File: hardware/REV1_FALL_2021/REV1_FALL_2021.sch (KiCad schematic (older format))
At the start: 22 parts, among them U1 Teensy3.6_All_Pins, U2 PA16165_Breakout, U3 MPL3115A2_Breakout, U4 BNO055_Breakout, U5 RFM69HCW_Breakout

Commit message: arrange and annotate schematic
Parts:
- removed BT? (x2): Battery_Cell, symbol Device:Battery_Cell
- removed C? (x2): C_0.1uF, symbol Device:C
- removed C?: C, symbol Device:C
- removed R?: R_250, symbol Device:R
- removed R?: R_15k, symbol Device:R
- removed R?: R_5k, symbol Device:R
- removed R?: R_10k, symbol Device:R
- removed U?: TPS2113ADRBR, IC_DRV8601DRBT, symbol TPS2113ADRBR:TPS2113ADRBR
- gave numbers to parts that had none: 7
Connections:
- net E-Match_Trigger_1 is gone; now on net E-MATCH_TRIGGER: R103.2
- net STAT is gone; now on net TPS_1_STAT: U1.32 (35_A16_PWM)
- net VIN is gone; now on net V_TEENSY: U1.53 (VIN)
- net BALANCE_CONTROL: now also U1.34 (37_A18_PWM_SCL1)
- net TPS_2_STAT: now also U1.33 (36_A17_PWM)
- net E-MATCH_TRIGGER: now reaches U1.36 (39_A20)
- no-connect marks 89 -> 88
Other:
- moved on the sheet: BT101, BT102, J101, Q101, R101, R102, R103, U1

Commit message: assign footprints to all but battery holders
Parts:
- R101, R102, R103: footprint (none) -> Resistor_SMD:R_0805_2012Metric_Pad1.20x1.40mm_HandSolder
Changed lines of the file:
@@
 F 0 "R103" V 19343 4400 50  0000 C CNN
 F 1 "R_10k" V 19434 4400 50  0000 C CNN
-F 2 "" V 19480 4400 50  0001 C CNN
+F 2 "Resistor_SMD:R_0805_2012Metric_Pad1.20x1.40mm_HandSolder" V 19480 4400 50  0001 C CNN
 F 3 "~" H 19550 4400 50  0001 C CNN
 	1    19550 4400
@@
 F 0 "R102" H 14220 6796 50  0000 L CNN
 F 1 "R_5k" H 13900 6750 50  0000 L CNN
-F 2 "" V 14080 6750 50  0001 C CNN
+F 2 "Resistor_SMD:R_0805_2012Metric_Pad1.20x1.40mm_HandSolder" V 14080 6750 50  0001 C CNN
 F 3 "~" H 14150 6750 50  0001 C CNN
 	1    14150 6750
@@
 F 0 "R101" H 14220 6196 50  0000 L CNN
 F 1 "R_15k" H 13850 6150 50  0000 L CNN
-F 2 "" V 14080 6150 50  0001 C CNN
+F 2 "Resistor_SMD:R_0805_2012Metric_Pad1.20x1.40mm_HandSolder" V 14080 6150 50  0001 C CNN
 F 3 "~" H 14150 6150 50  0001 C CNN
 	1    14150 6150

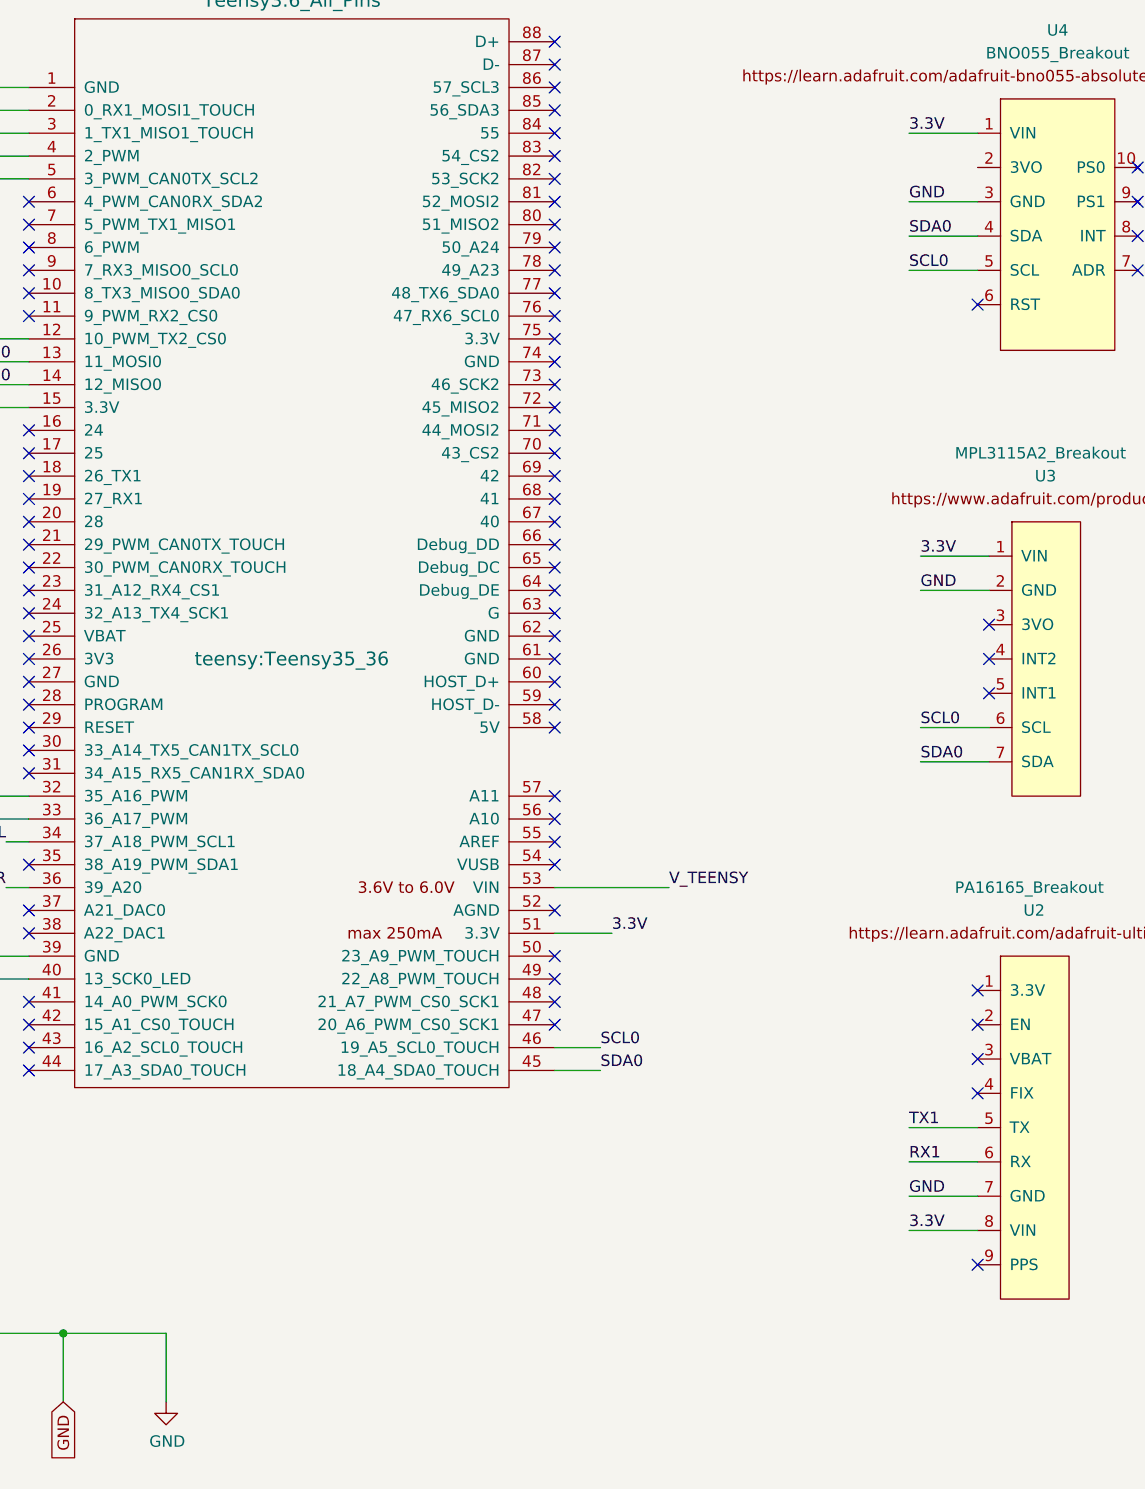
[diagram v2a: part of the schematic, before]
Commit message: import and associate battery footprint
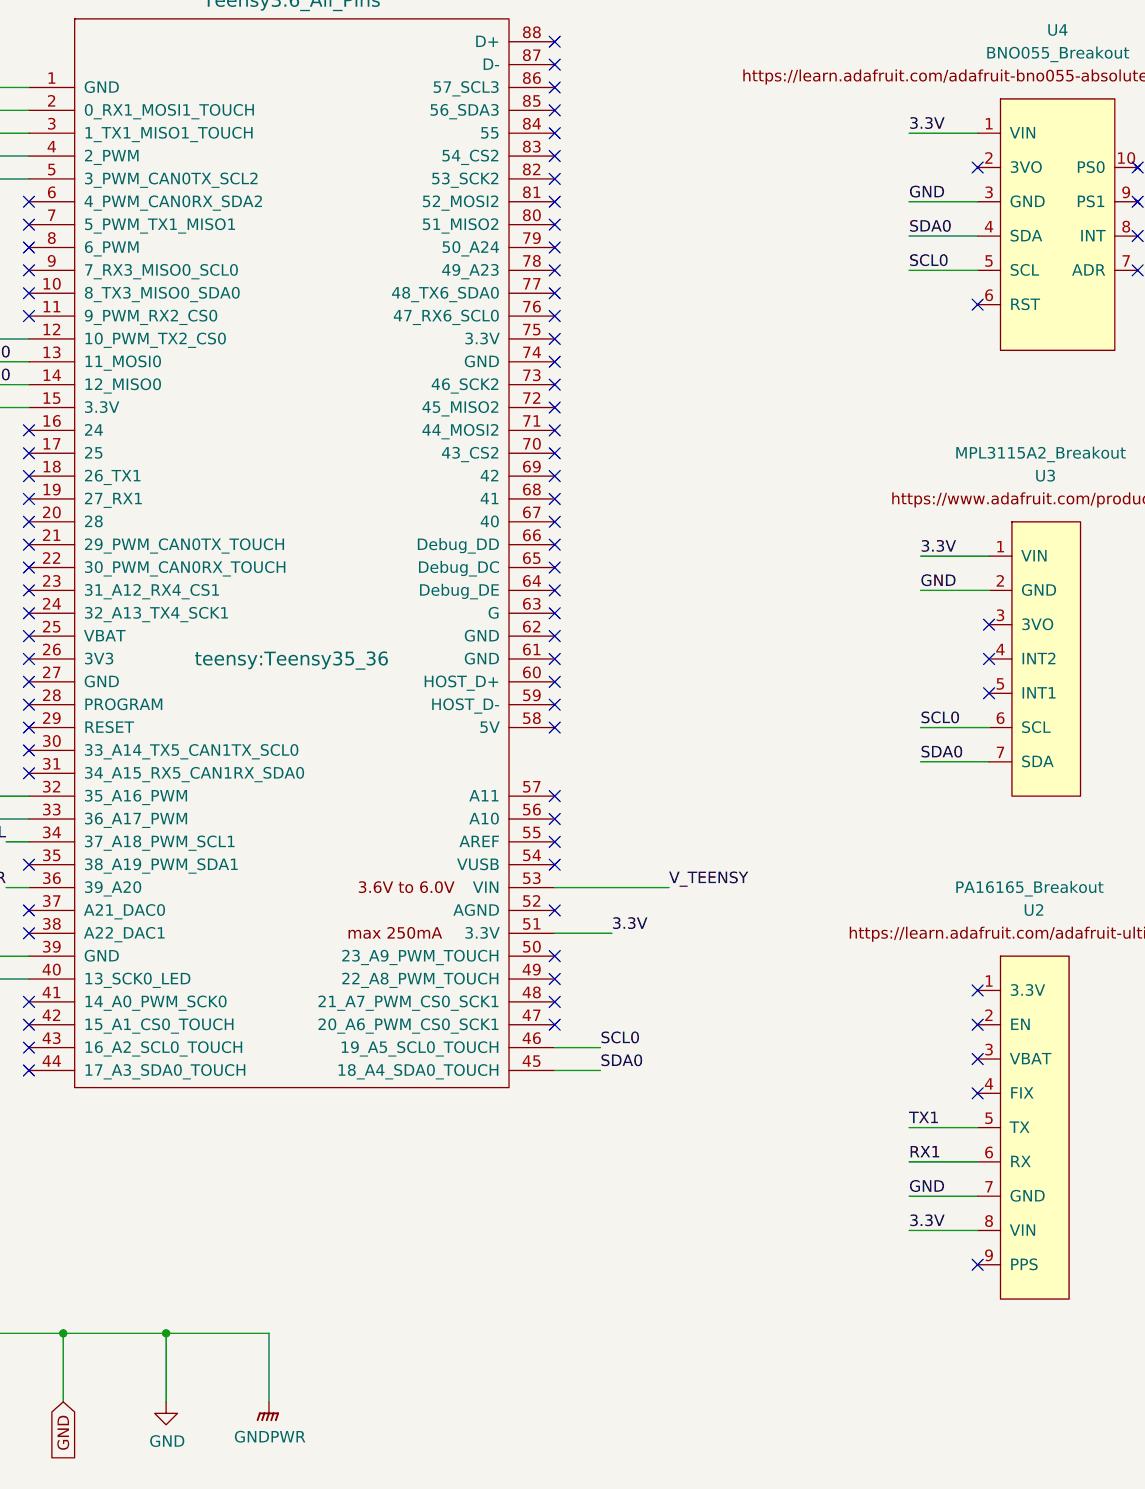
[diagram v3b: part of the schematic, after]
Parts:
- BT101, BT102: footprint (none) -> Olin_Rocketry:MyBatteryHolder_MPD_BH-18650-PC2
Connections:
- no-connect marks 88 -> 89
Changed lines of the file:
@@
 F 0 "BT101" H 12968 4446 50  0000 L CNN
 F 1 "Battery_Cell" H 12968 4355 50  0000 L CNN
-F 2 "" V 12850 4410 50  0001 C CNN
+F 2 "Olin_Rocketry:MyBatteryHolder_MPD_BH-18650-PC2" V 12850 4410 50  0001 C CNN
 F 3 "~" V 12850 4410 50  0001 C CNN
 	1    12850 4350
@@
 F 0 "BT102" H 13018 3596 50  0000 L CNN
 F 1 "Battery_Cell" H 13018 3505 50  0000 L CNN
-F 2 "" V 12900 3560 50  0001 C CNN
+F 2 "Olin_Rocketry:MyBatteryHolder_MPD_BH-18650-PC2" V 12900 3560 50  0001 C CNN
 F 3 "~" V 12900 3560 50  0001 C CNN
 	1    12900 3500
@@
 NoConn ~ 3750 2550
 NoConn ~ 3750 2650
+NoConn ~ 5600 1800
+$Comp
+L power:GNDPWR #PWR0101
+U 1 1 61B2C185
+P 2500 7200
+F 0 "#PWR0101" H 2500 7000 50  0001 C CNN
+F 1 "GNDPWR" H 2504 7046 50  0000 C CNN
+F 2 "" H 2500 7150 50  0001 C CNN
+F 3 "" H 2500 7150 50  0001 C CNN
+	1    2500 7200
+	1    0    0    -1
+$EndComp
+Wire Wire Line
+	2500 7200 2500 6900
+Wire Wire Line
+	2500 6900 2050 6900
+Connection ~ 2050 6900
 $EndSCHEMATC

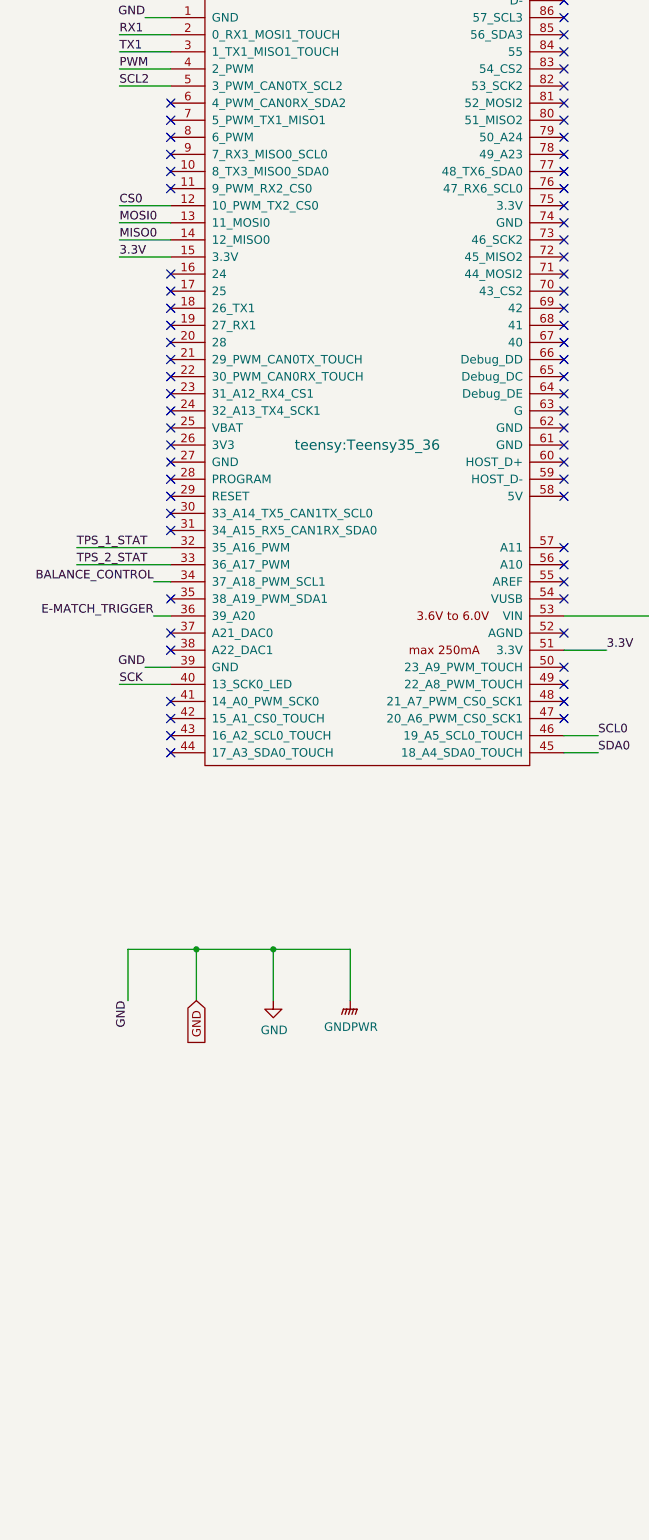
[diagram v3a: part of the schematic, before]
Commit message: add LEDs to schematic
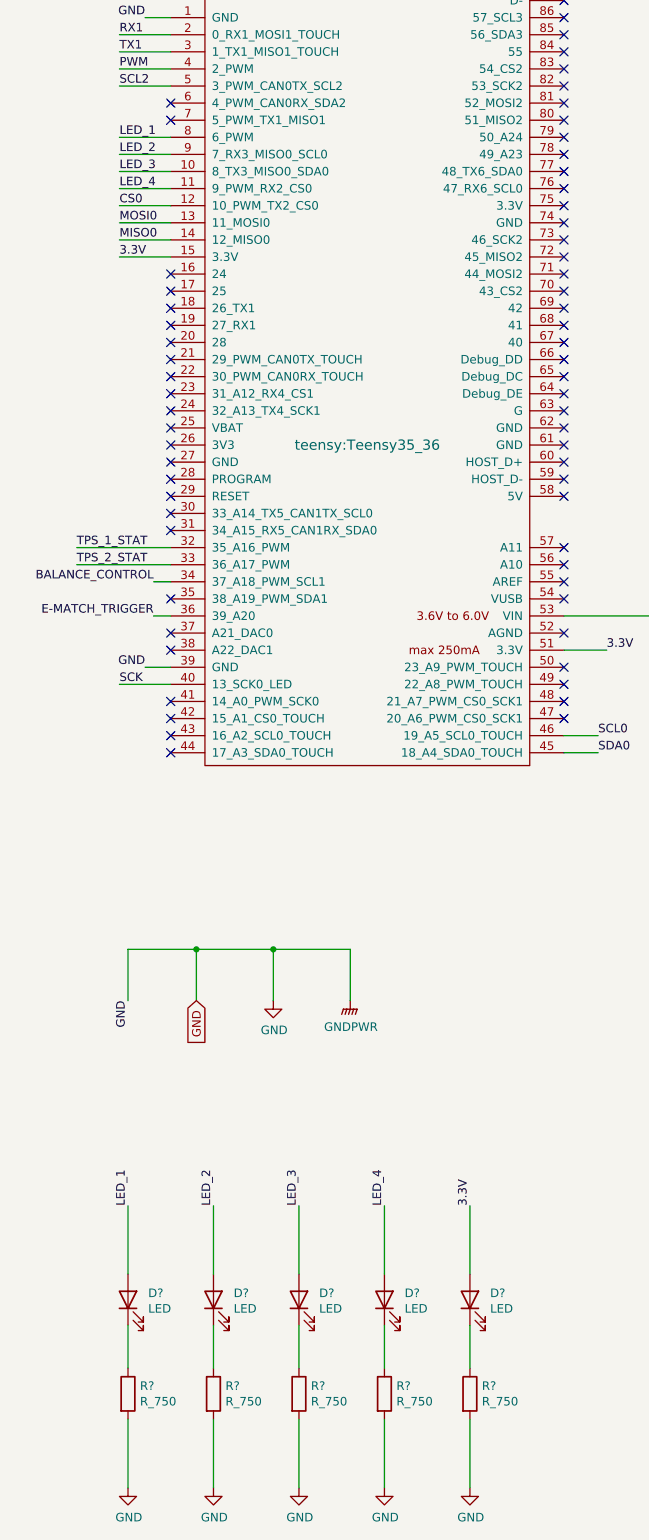
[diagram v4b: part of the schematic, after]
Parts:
- added D? (x5): LED, LED_SMD:LED_0805_2012Metric_Pad1.15x1.40mm_HandSolder, symbol Device:LED
- added R? (x5): R_750, Resistor_SMD:R_0805_2012Metric_Pad1.20x1.40mm_HandSolder, symbol Device:R
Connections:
- net 3.3V: now also D?.2 (A)
- net GND: now also R?.2, R?.2, R?.2, R?.2, R?.2
- net LED_3: now reaches U1.10 (8_TX3_MISO0_SDA0)
- net LED_3: now also D?.2 (A)
- net LED_4: now reaches U1.11 (9_PWM_RX2_CS0)
- net LED_4: now also D?.2 (A)
- net LED_1: now reaches U1.8 (6_PWM)
- net LED_1: now also D?.2 (A)
- net LED_2: now reaches U1.9 (7_RX3_MISO0_SCL0)
- net LED_2: now also D?.2 (A)
- new net: D?.1 (K), R?.1 (x5)
- no-connect marks 89 -> 85
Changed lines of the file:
@@
 NoConn ~ 1450 1950
 NoConn ~ 1450 2050
-NoConn ~ 1450 2150
-NoConn ~ 1450 2250
-NoConn ~ 1450 2350
-NoConn ~ 1450 2450
 NoConn ~ 1450 2950
 NoConn ~ 1450 3050
@@
 	2500 6900 2050 6900
 Connection ~ 2050 6900
+$Comp
+L Device:LED D?
+U 1 1 619C7C94
+P 1200 8950
+F 0 "D?" V 1239 8832 50  0000 R CNN
+F 1 "LED" V 1148 8832 50  0000 R CNN
+F 2 "LED_SMD:LED_0805_2012Metric_Pad1.15x1.40mm_HandSolder" H 1200 8950 50  0001 C CNN
+F 3 "https://datasheet.lcsc.com/lcsc/1806130620_Hubei-KENTO-Elec-C2293_C2293.pdf" H 1200 8950 50  0001 C CNN
+	1    1200 8950
+	0    -1   -1   0
+$EndComp
+$Comp
+L Device:R R?
+U 1 1 619CBBB6
+P 1200 9500
+F 0 "R?" H 1270 9546 50  0000 L CNN
+F 1 "R_750" H 1270 9455 50  0000 L CNN
+F 2 "Resistor_SMD:R_0805_2012Metric_Pad1.20x1.40mm_HandSolder" V 1130 9500 50  0001 C CNN
+F 3 "~" H 1200 9500 50  0001 C CNN
+	1    1200 9500
+	1    0    0    -1
+$EndComp
+Wire Wire Line
+	1200 9100 1200 9350
+Text Label 1200 8400 1    50   ~ 0
+LED_1
+Wire Wire Line
+	1200 8400 1200 8800
+Wire Wire Line
+	1200 9650 1200 10050
+$Comp
+L power:GND #PWR?
+U 1 1 619E5D47
+P 1200 10050
+F 0 "#PWR?" H 1200 9800 50  0001 C CNN
+F 1 "GND" H 1205 9877 50  0000 C CNN
+F 2 "" H 1200 10050 50  0001 C CNN
+F 3 "" H 1200 10050 50  0001 C CNN
+	1    1200 10050
+	1    0    0    -1
+$EndComp
+$Comp
+L Device:LED D?
+U 1 1 619E9614
+P 1700 8950
+F 0 "D?" V 1739 8832 50  0000 R CNN
+F 1 "LED" V 1648 8832 50  0000 R CNN
+F 2 "LED_SMD:LED_0805_2012Metric_Pad1.15x1.40mm_HandSolder" H 1700 8950 50  0001 C CNN
+F 3 "https://datasheet.lcsc.com/lcsc/1806130620_Hubei-KENTO-Elec-C2293_C2293.pdf" H 1700 8950 50  0001 C CNN
+	1    1700 8950
+	0    -1   -1   0
+$EndComp
+$Comp
+L Device:R R?
+U 1 1 619E961A
+P 1700 9500
+F 0 "R?" H 1770 9546 50  0000 L CNN
+F 1 "R_750" H 1770 9455 50  0000 L CNN
+F 2 "Resistor_SMD:R_0805_2012Metric_Pad1.20x1.40mm_HandSolder" V 1630 9500 50  0001 C CNN
+F 3 "~" H 1700 9500 50  0001 C CNN
+	1    1700 9500
+	1    0    0    -1
+$EndComp
+Wire Wire Line
+	1700 9100 1700 9350
+Text Label 1700 8400 1    50   ~ 0
+LED_2
+Wire Wire Line
+	1700 8400 1700 8800
+Wire Wire Line
+	1700 9650 1700 10050
+$Comp
+L power:GND #PWR?
+U 1 1 619E9624
+P 1700 10050
+F 0 "#PWR?" H 1700 9800 50  0001 C CNN
+F 1 "GND" H 1705 9877 50  0000 C CNN
+F 2 "" H 1700 10050 50  0001 C CNN
+F 3 "" H 1700 10050 50  0001 C CNN
+	1    1700 10050
+	1    0    0    -1
+$EndComp
+$Comp
+L Device:LED D?
+U 1 1 619EBAF0
+P 2200 8950
+F 0 "D?" V 2239 8832 50  0000 R CNN
+F 1 "LED" V 2148 8832 50  0000 R CNN
+F 2 "LED_SMD:LED_0805_2012Metric_Pad1.15x1.40mm_HandSolder" H 2200 8950 50  0001 C CNN
+F 3 "https://datasheet.lcsc.com/lcsc/1806130620_Hubei-KENTO-Elec-C2293_C2293.pdf" H 2200 8950 50  0001 C CNN
+	1    2200 8950
+	0    -1   -1   0
+$EndComp
+$Comp
+L Device:R R?
+U 1 1 619EBAF6
+P 2200 9500
+F 0 "R?" H 2270 9546 50  0000 L CNN
+F 1 "R_750" H 2270 9455 50  0000 L CNN
+F 2 "Resistor_SMD:R_0805_2012Metric_Pad1.20x1.40mm_HandSolder" V 2130 9500 50  0001 C CNN
+F 3 "~" H 2200 9500 50  0001 C CNN
+	1    2200 9500
+	1    0    0    -1
+$EndComp
+Wire Wire Line
+	2200 9100 2200 9350
+Text Label 2200 8400 1    50   ~ 0
+LED_3
+Wire Wire Line
+	2200 8400 2200 8800
+Wire Wire Line
+	2200 9650 2200 10050
+$Comp
+L power:GND #PWR?
+U 1 1 619EBB00
+P 2200 10050
+F 0 "#PWR?" H 2200 9800 50  0001 C CNN
+F 1 "GND" H 2205 9877 50  0000 C CNN
+F 2 "" H 2200 10050 50  0001 C CNN
+F 3 "" H 2200 10050 50  0001 C CNN
+	1    2200 10050
+	1    0    0    -1
+$EndComp
+$Comp
+L Device:LED D?
+U 1 1 619EE1C7
+P 2700 8950
+F 0 "D?" V 2739 8832 50  0000 R CNN
+F 1 "LED" V 2648 8832 50  0000 R CNN
+F 2 "LED_SMD:LED_0805_2012Metric_Pad1.15x1.40mm_HandSolder" H 2700 8950 50  0001 C CNN
+F 3 "https://datasheet.lcsc.com/lcsc/1806130620_Hubei-KENTO-Elec-C2293_C2293.pdf" H 2700 8950 50  0001 C CNN
+	1    2700 8950
+	0    -1   -1   0
+$EndComp
+$Comp
+L Device:R R?
+U 1 1 619EE1CD
+P 2700 9500
+F 0 "R?" H 2770 9546 50  0000 L CNN
+F 1 "R_750" H 2770 9455 50  0000 L CNN
+F 2 "Resistor_SMD:R_0805_2012Metric_Pad1.20x1.40mm_HandSolder" V 2630 9500 50  0001 C CNN
+F 3 "~" H 2700 9500 50  0001 C CNN
+	1    2700 9500
+	1    0    0    -1
+$EndComp
+Wire Wire Line
+	2700 9100 2700 9350
+Text Label 2700 8400 1    50   ~ 0
+LED_4
+Wire Wire Line
+	2700 8400 2700 8800
+Wire Wire Line
+	2700 9650 2700 10050
+$Comp
+L power:GND #PWR?
+U 1 1 619EE1D7
+P 2700 10050
+F 0 "#PWR?" H 2700 9800 50  0001 C CNN
+F 1 "GND" H 2705 9877 50  0000 C CNN
+F 2 "" H 2700 10050 50  0001 C CNN
+F 3 "" H 2700 10050 50  0001 C CNN
+	1    2700 10050
+	1    0    0    -1
+$EndComp
+$Comp
+L Device:LED D?
+U 1 1 619F098B
+P 3200 8950
+F 0 "D?" V 3239 8832 50  0000 R CNN
+F 1 "LED" V 3148 8832 50  0000 R CNN
+F 2 "LED_SMD:LED_0805_2012Metric_Pad1.15x1.40mm_HandSolder" H 3200 8950 50  0001 C CNN
+F 3 "https://datasheet.lcsc.com/lcsc/1806130620_Hubei-KENTO-Elec-C2293_C2293.pdf" H 3200 8950 50  0001 C CNN
+	1    3200 8950
+	0    -1   -1   0
+$EndComp
+$Comp
+L Device:R R?
+U 1 1 619F0991
+P 3200 9500
+F 0 "R?" H 3270 9546 50  0000 L CNN
+F 1 "R_750" H 3270 9455 50  0000 L CNN
+F 2 "Resistor_SMD:R_0805_2012Metric_Pad1.20x1.40mm_HandSolder" V 3130 9500 50  0001 C CNN
+F 3 "~" H 3200 9500 50  0001 C CNN
+	1    3200 9500
+	1    0    0    -1
+$EndComp
+Wire Wire Line
+	3200 9100 3200 9350
+Wire Wire Line
+	3200 8400 3200 8800
+Wire Wire Line
+	3200 9650 3200 10050
+$Comp
+L power:GND #PWR?
+U 1 1 619F099B
+P 3200 10050
+F 0 "#PWR?" H 3200 9800 50  0001 C CNN
+F 1 "GND" H 3205 9877 50  0000 C CNN
+F 2 "" H 3200 10050 50  0001 C CNN
+F 3 "" H 3200 10050 50  0001 C CNN
+	1    3200 10050
+	1    0    0    -1
+$EndComp
+Text Label 1150 2150 0    50   ~ 0
+LED_1
+Wire Wire Line
+	1450 2150 1150 2150
+Text Label 1150 2250 0    50   ~ 0
+LED_2
+Text Label 1150 2350 0    50   ~ 0
+LED_3
+Text Label 1150 2450 0    50   ~ 0
+LED_4
+Wire Wire Line
+	1450 2250 1150 2250
+Wire Wire Line
+	1450 2350 1150 2350
+Wire Wire Line
+	1450 2450 1150 2450
+Text Label 3200 8400 1    50   ~ 0
+3.3V
 $EndSCHEMATC
